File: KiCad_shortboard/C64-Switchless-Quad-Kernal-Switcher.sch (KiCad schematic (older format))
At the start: 10 parts, among them J1 01x14_precision_pinlist, J2 01x14_precision_pinlist, J3 27C256/512_28PDIP, J4 Wireconnections, U1 ATtiny85-20PU, U2 74LS08

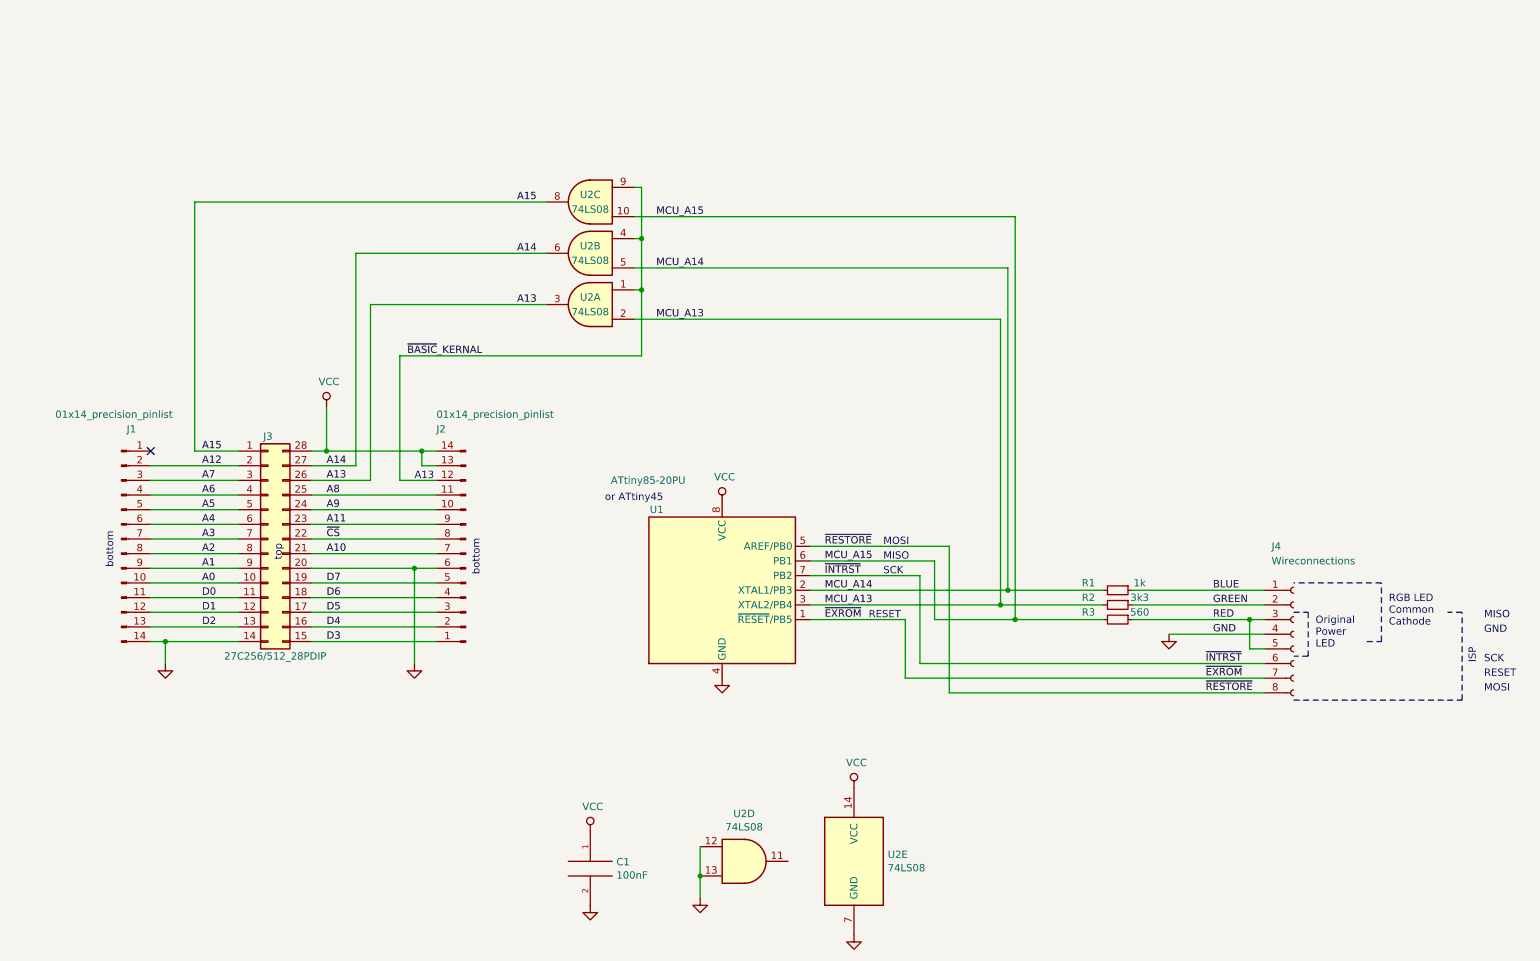
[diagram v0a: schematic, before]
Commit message: shortboard version schematics added to user guide
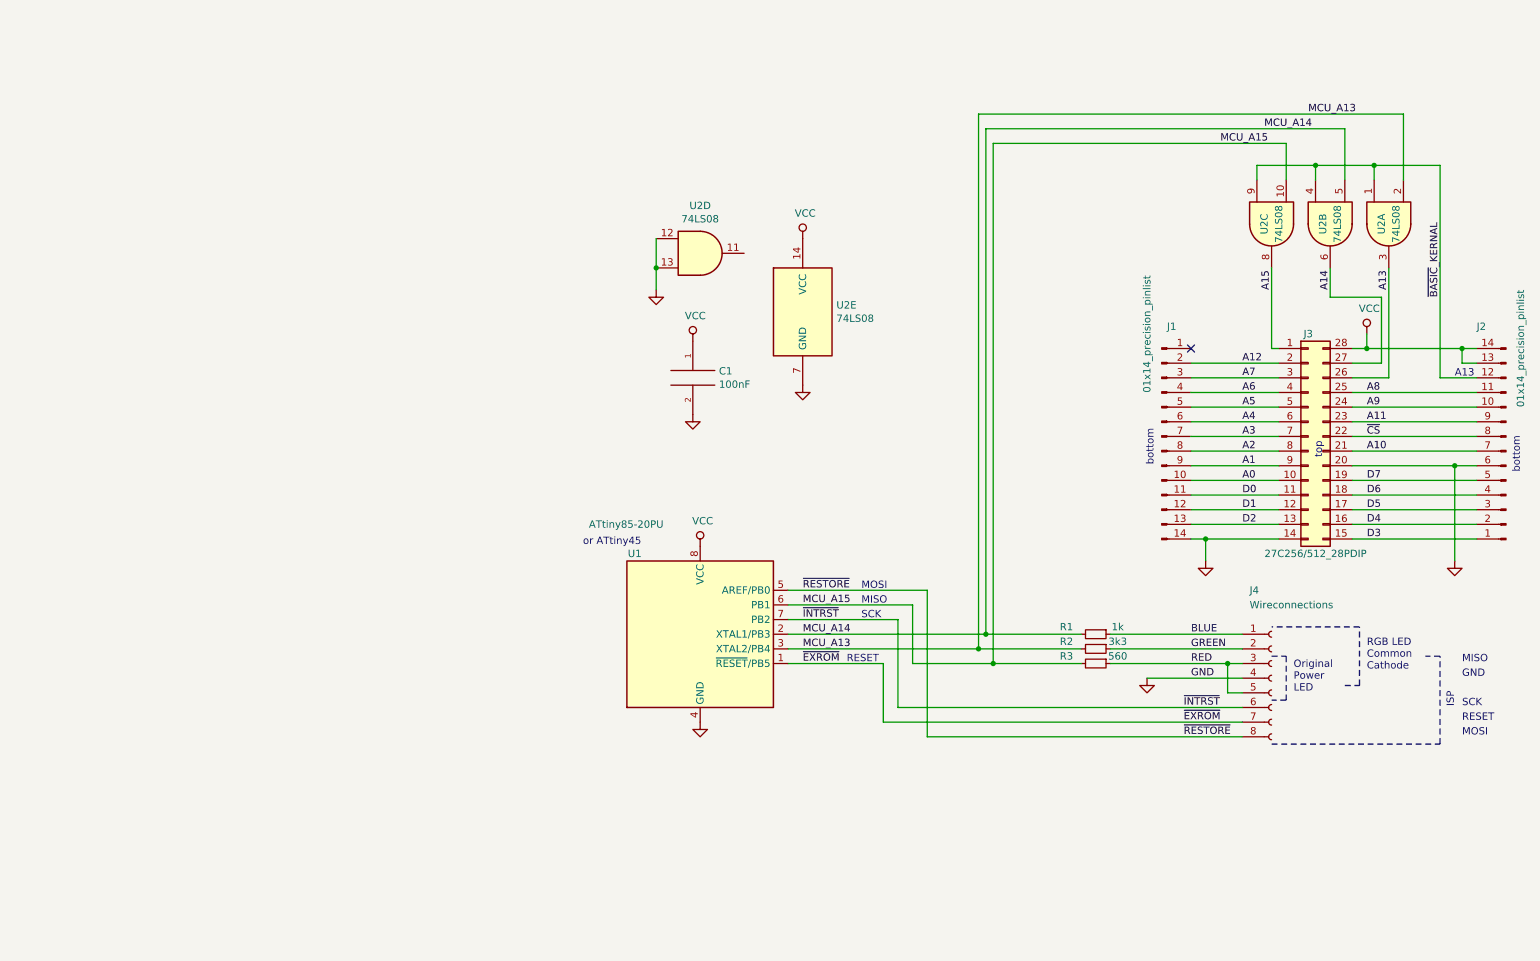
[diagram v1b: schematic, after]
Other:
- moved on the sheet: C1, J1, J2, J3, J4, R1, R2, R3, U1, U2A, U2B, U2C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

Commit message: 1541C support in firmware and SKS64 shortboard pcb version
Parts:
- added JP1, JP2, JP3, JP4: SolderJumper_2_Open, pkl_jumpers:J_0402, symbol Jumper:SolderJumper_2_Open
- U1: symbol MCU_Microchip_ATtiny:ATtiny85-20PU -> C64-Switchless-Quad-Kernal-Switcher-rescue:ATtiny85-20PU-MCU_Microchip_ATtiny
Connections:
- net A13: now also JP3.1 (A), JP4.1 (A)
- net A14: now also JP2.1 (A)
- net A15: now also JP1.1 (A)
- net MCU_A13: now also JP3.2 (B)
- net MCU_A14: now also JP2.2 (B)
- net MCU_A15: now also JP1.2 (B)
- net ~BASIC~_KERNAL: now also JP4.2 (B)
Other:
- note added: "1541C/1541II 16K"
- note added: "C64 shortboard"
- note added: "JP1 JP2 JP3 JP4 U2"
- note added: "Mode"
- note added: "x"
- moved on the sheet: U2B, U2C
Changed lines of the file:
@@
 EESchema Schematic File Version 4
-LIBS:C64-Switchless-Quad-Kernal-Switcher-cache
-EELAYER 29 0
+EELAYER 30 0
 EELAYER END
 $Descr A4 11693 8268
@@
 Sheet 1 1
 Title "C64 Switchless Quad Kernal Switcher - shortboard"
-Date "2019-07-18"
-Rev "1.0"
+Date "2021-08-10"
+Rev "1.1"
 Comp "Bwack"
-Comment1 "C64 Short motherboard version"
-Comment2 "must include basic image at first 8k bank"
-Comment3 "Ideas from Sven Petersen's switcher"
-Comment4 ""
+Comment1 "C64 Short motherboard version. 28-28pin board."
+Comment2 "Ideas from Sven Petersen's switcher."
+Comment3 "C64 shortboard: Add U2, and include BASIC image at bank0 in a *256 or *512 ROM."
+Comment4 "1541C/1541-II mode: Do not add U2. Add solder to JP1, JP2 and JP4. Use *256 ROM."
 $EndDescr
 $Comp
@@
 L power:VCC #PWR0102
 U 1 1 5D2C04ED
-P 9850 3500
-F 0 "#PWR0102" H 9850 3350 50  0001 C CNN
-F 1 "VCC" H 9867 3673 50  0000 C CNN
-F 2 "" H 9850 3500 50  0001 C CNN
-F 3 "" H 9850 3500 50  0001 C CNN
-	1    9850 3500
+P 10500 3500
+F 0 "#PWR0102" H 10500 3350 50  0001 C CNN
+F 1 "VCC" H 10517 3673 50  0000 C CNN
+F 2 "" H 10500 3500 50  0001 C CNN
+F 3 "" H 10500 3500 50  0001 C CNN
+	1    10500 3500
 	1    0    0    -1
 $EndComp
@@
 	5900 5350 6750 5350
 $Comp
-L MCU_Microchip_ATtiny:ATtiny85-20PU U1
+L C64-Switchless-Quad-Kernal-Switcher-rescue:ATtiny85-20PU-MCU_Microchip_ATtiny U1
 U 1 1 5D2A0255
 P 5300 5550
@@
 	1    0    0    -1
 $EndComp
-Wire Wire Line
-	9750 3600 9850 3600
 Wire Wire Line
 	9750 3900 10600 3900
@@
 Wire Wire Line
 	8750 4900 9250 4900
-Wire Wire Line
-	9850 3600 9850 3500
-Connection ~ 9850 3600
-Wire Wire Line
-	9850 3600 10500 3600
 Wire Wire Line
 	8750 5050 8750 4900
@@
 NoConn ~ 8650 3600
 Wire Wire Line
-	9250 3600 9200 3600
+	9250 3600 8800 3600
 Wire Wire Line
 	9250 3700 8650 3700
@@
 	10500 3600 10600 3600
 Wire Wire Line
-	9750 3700 9950 3700
-Wire Wire Line
 	10350 3800 10600 3800
-Text Label 10350 3250 1    50   ~ 0
+Text Label 10600 3050 1    50   ~ 0
 ~BASIC~_KERNAL
 Text Notes 10450 3800 0    50   ~ 0
 A13
-Text Label 9200 3200 1    50   ~ 0
+Text Label 8800 3450 1    50   ~ 0
 A15
-Text Label 9600 3200 1    50   ~ 0
+Text Label 9850 3450 1    50   ~ 0
 A14
-Text Label 10000 3200 1    50   ~ 0
+Text Label 10000 3450 1    50   ~ 0
 A13
 $Comp
@@
 L 74xx:74LS08 U2
 U 2 1 5D40257B
-P 9600 2750
-F 0 "U2" H 9600 2800 50  0000 C CNN
-F 1 "74LS08" H 9600 2700 50  0000 C CNN
-F 2 "Package_SO:SOIC-14_3.9x8.7mm_P1.27mm" H 9600 2750 50  0001 C CNN
-F 3 "http://www.ti.com/lit/gpn/sn74LS08" H 9600 2750 50  0001 C CNN
-	2    9600 2750
-	0    -1   1    0
-$EndComp
-$Comp
-L 74xx:74LS08 U2
-U 3 1 5D418CB3
-P 9200 2750
-F 0 "U2" H 9200 2800 50  0000 C CNN
-F 1 "74LS08" H 9200 2700 50  0000 C CNN
-F 2 "Package_SO:SOIC-14_3.9x8.7mm_P1.27mm" H 9200 2750 50  0001 C CNN
-F 3 "http://www.ti.com/lit/gpn/sn74LS08" H 9200 2750 50  0001 C CNN
-	3    9200 2750
+P 9400 2750
+F 0 "U2" H 9400 2800 50  0000 C CNN
+F 1 "74LS08" H 9400 2700 50  0000 C CNN
+F 2 "Package_SO:SOIC-14_3.9x8.7mm_P1.27mm" H 9400 2750 50  0001 C CNN
+F 3 "http://www.ti.com/lit/gpn/sn74LS08" H 9400 2750 50  0001 C CNN
+	2    9400 2750
 	0    -1   1    0
 $EndComp
@@
 Wire Wire Line
 	7300 5750 7900 5750
-Text Label 8850 2200 0    50   ~ 0
-MCU_A15
-Text Label 9450 2000 0    50   ~ 0
+Text Label 9750 2000 0    50   ~ 0
 MCU_A13
 Text Label 9150 2100 0    50   ~ 0
 MCU_A14
 Wire Wire Line
-	9950 3700 9950 3250
-Wire Wire Line
-	9950 3250 9600 3250
-Wire Wire Line
-	9600 3250 9600 3050
-Wire Wire Line
-	9200 3600 9200 3050
-Wire Wire Line
-	10000 3050 10000 3800
-Wire Wire Line
-	10350 2350 9900 2350
-Wire Wire Line
-	9100 2350 9100 2450
-Wire Wire Line
-	9500 2450 9500 2350
-Connection ~ 9500 2350
-Wire Wire Line
-	9500 2350 9100 2350
+	9400 3250 9400 3100
+Wire Wire Line
+	10000 3050 10000 3100
+Wire Wire Line
+	9300 2450 9300 2350
+Connection ~ 9300 2350
 Wire Wire Line
 	9900 2450 9900 2350
 Connection ~ 9900 2350
 Wire Wire Line
-	9900 2350 9500 2350
-Wire Wire Line
-	10350 2350 10350 3800
-Wire Wire Line
-	7300 2200 9300 2200
-Wire Wire Line
-	9300 2200 9300 2450
-Wire Wire Line
-	7250 2100 9700 2100
-Wire Wire Line
-	9700 2100 9700 2450
+	9900 2350 9300 2350
+Wire Wire Line
+	7250 2100 9500 2100
+Wire Wire Line
+	9500 2100 9500 2450
 Wire Wire Line
 	7200 2000 10100 2000
@@
 Wire Wire Line
 	5900 5550 7250 5550
+$Comp
+L Jumper:SolderJumper_2_Open JP4
+U 1 1 61108399
+P 10200 3800
+F 0 "JP4" H 10200 3913 50  0000 C CNN
+F 1 "SolderJumper_2_Open" H 10200 3914 50  0001 C CNN
+F 2 "pkl_jumpers:J_0402" H 10200 3800 50  0001 C CNN
+F 3 "~" H 10200 3800 50  0001 C CNN
+	1    10200 3800
+	1    0    0    -1
+$EndComp
+Connection ~ 10350 3800
+Wire Wire Line
+	10050 3800 10000 3800
+Connection ~ 10000 3800
+Wire Wire Line
+	10500 3600 10500 3500
+Wire Wire Line
+	9750 3600 10500 3600
+Text Label 8550 2200 0    50   ~ 0
+MCU_A15
+Wire Wire Line
+	7300 2200 8900 2200
+Wire Wire Line
+	9300 2350 8700 2350
+Wire Wire Line
+	8700 2350 8700 2450
+Wire Wire Line
+	8800 3600 8800 3100
+Wire Wire Line
+	8900 2200 8900 2450
+$Comp
+L 74xx:74LS08 U2
+U 3 1 5D418CB3
+P 8800 2750
+F 0 "U2" H 8800 2800 50  0000 C CNN
+F 1 "74LS08" H 8800 2700 50  0000 C CNN
+F 2 "Package_SO:SOIC-14_3.9x8.7mm_P1.27mm" H 8800 2750 50  0001 C CNN
+F 3 "http://www.ti.com/lit/gpn/sn74LS08" H 8800 2750 50  0001 C CNN
+	3    8800 2750
+	0    -1   1    0
+$EndComp
+Wire Wire Line
+	9850 3250 9400 3250
+Wire Wire Line
+	9750 3700 9850 3700
+Wire Wire Line
+	9850 3700 9850 3250
+$Comp
+L Jumper:SolderJumper_2_Open JP1
+U 1 1 611634FF
+P 8950 3100
+F 0 "JP1" H 8950 3213 50  0000 C CNN
+F 1 "SolderJumper_2_Open" H 8950 3214 50  0001 C CNN
+F 2 "pkl_jumpers:J_0402" H 8950 3100 50  0001 C CNN
+F 3 "~" H 8950 3100 50  0001 C CNN
+	1    8950 3100
+	1    0    0    -1
+$EndComp
+Connection ~ 8800 3100
+Wire Wire Line
+	8800 3100 8800 3050
+Wire Wire Line
+	9100 3100 9100 2450
+Wire Wire Line
+	9100 2450 8900 2450
+Connection ~ 8900 2450
+$Comp
+L Jumper:SolderJumper_2_Open JP2
+U 1 1 611BCCC7
+P 9550 3100
+F 0 "JP2" H 9550 3213 50  0000 C CNN
+F 1 "SolderJumper_2_Open" H 9550 3214 50  0001 C CNN
+F 2 "pkl_jumpers:J_0402" H 9550 3100 50  0001 C CNN
+F 3 "~" H 9550 3100 50  0001 C CNN
+	1    9550 3100
+	1    0    0    -1
+$EndComp
+Connection ~ 9400 3100
+Wire Wire Line
+	9400 3100 9400 3050
+Wire Wire Line
+	9700 3100 9700 2450
+Wire Wire Line
+	9700 2450 9500 2450
+Connection ~ 9500 2450
+Wire Wire Line
+	10350 3250 10600 3250
+Wire Wire Line
+	10600 3250 10600 2350
+Wire Wire Line
+	10350 3250 10350 3800
+Wire Wire Line
+	9900 2350 10600 2350
+$Comp
+L Jumper:SolderJumper_2_Open JP3
+U 1 1 611C8E9A
+P 10150 3100
+F 0 "JP3" H 10150 3213 50  0000 C CNN
+F 1 "SolderJumper_2_Open" H 10150 3214 50  0001 C CNN
+F 2 "pkl_jumpers:J_0402" H 10150 3100 50  0001 C CNN
+F 3 "~" H 10150 3100 50  0001 C CNN
+	1    10150 3100
+	1    0    0    -1
+$EndComp
+Connection ~ 10000 3100
+Wire Wire Line
+	10000 3100 10000 3800
+Wire Wire Line
+	10300 3100 10300 2450
+Wire Wire Line
+	10300 2450 10100 2450
+Connection ~ 10100 2450
+Text Notes 9600 1400 0    50   ~ 0
+JP1  JP2  JP3  JP4  U2
+Text Notes 8850 1500 0    50   ~ 0
+C64 shortboard
+Text Notes 9650 1600 0    50   ~ 0
+x
+Text Notes 9850 1600 0    50   ~ 0
+x
+Text Notes 10300 1600 0    50   ~ 0
+x
+Wire Notes Line style solid
+	10650 1300 10650 1600
+Wire Notes Line style solid
+	8750 1600 8750 1300
+Wire Notes Line style solid
+	8750 1300 10650 1300
+Wire Notes Line style solid
+	8750 1400 10650 1400
+Wire Notes Line style solid
+	9550 1300 9550 1600
+Wire Notes Line style solid
+	8750 1600 10650 1600
+Text Notes 9050 1400 0    50   ~ 0
+Mode
+Text Notes 8800 1600 0    50   ~ 0
+1541C/1541II 16K
+Text Notes 10500 1500 0    50   ~ 0
+x
+Wire Notes Line
+	10650 1500 8750 1500
 $EndSCHEMATC
